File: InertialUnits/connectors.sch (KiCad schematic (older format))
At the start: 2 parts, among them P1 CONN_2, P2 CONN_2

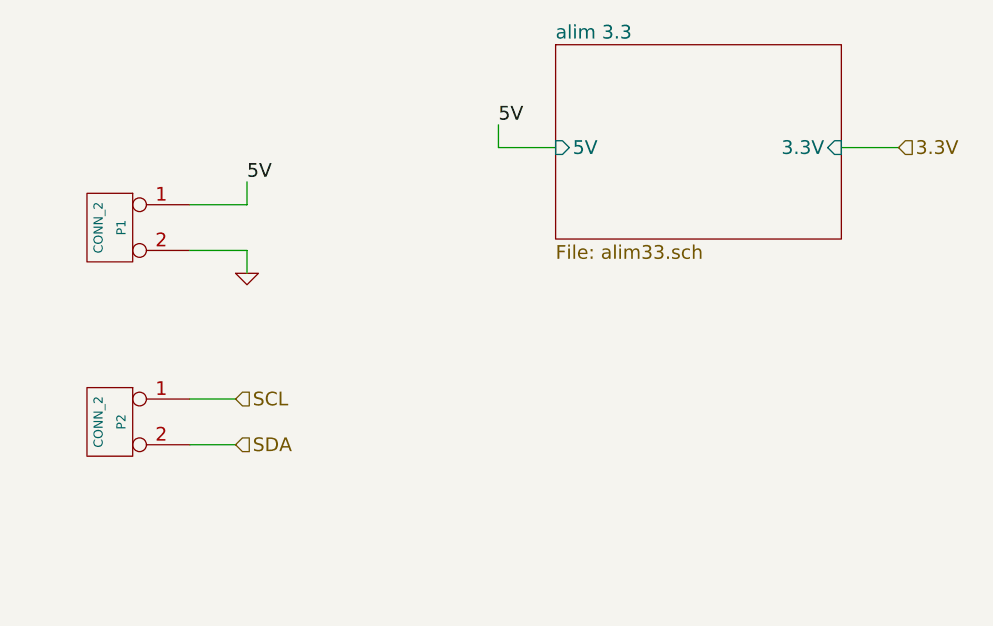
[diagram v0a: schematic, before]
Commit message: Modification axis on Inertial sensors
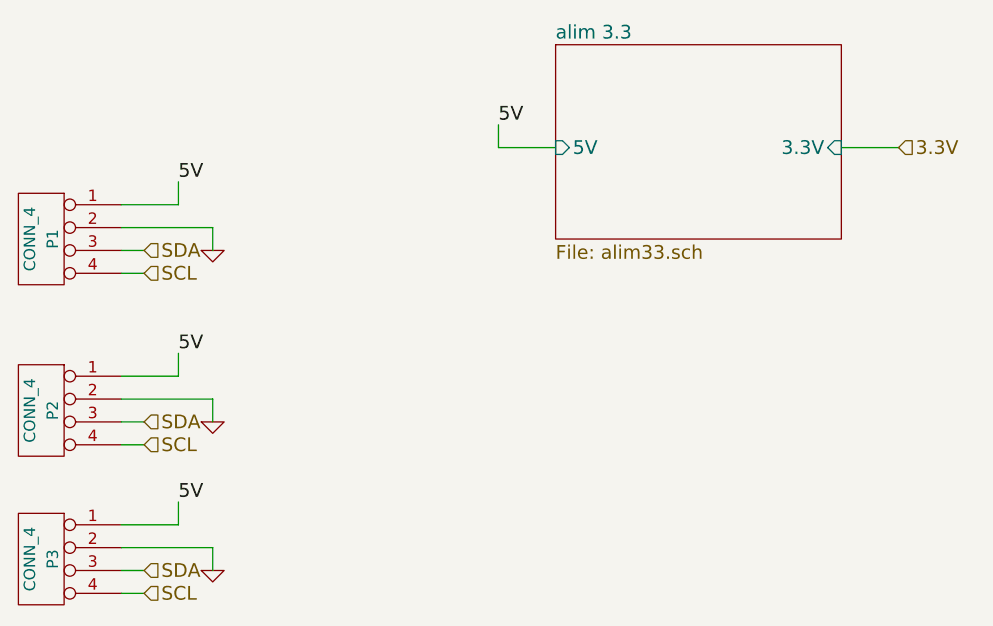
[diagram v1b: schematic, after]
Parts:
- removed P1, P2: CONN_2, symbol CONN_2
- added P1, P2, P3: CONN_4, symbol CONN_4
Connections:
- net 5V: now also P1.1 (P1), P2.1 (P1), P3.1 (P1)
- net GND: now also P1.2 (P2), P2.2 (P2), P3.2 (P2)
- net SCL: now also P1.4 (P4), P2.4 (P4), P3.4 (P4)
- net SDA: now also P1.3 (P3), P2.3 (P3), P3.3 (P3)
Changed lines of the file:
@@
-EESchema Schematic File Version 2  date lun. 31 mars 2014 21:58:22 CEST
+EESchema Schematic File Version 2
 LIBS:power
 LIBS:device
@@
 LIBS:perso
 LIBS:inertialSensors-cache
-EELAYER 25  0
+EELAYER 24 0
 EELAYER END
-$Descr A4 11700 8267
+$Descr A4 11693 8268
 encoding utf-8
 Sheet 2 4
@@
 	4500 2600 4750 2600
 Wire Wire Line
-	1650 3900 1850 3900
+	1350 3150 1450 3150
 Wire Wire Line
-	1900 3150 1900 3050
+	1750 3050 1750 2950
 Wire Wire Line
-	1900 3050 1650 3050
+	1750 2950 1350 2950
 Wire Wire Line
-	1650 2850 1900 2850
+	1350 2850 1600 2850
 Wire Wire Line
-	1900 2850 1900 2750
+	1600 2850 1600 2750
 Wire Wire Line
-	1650 3700 1850 3700
+	1350 3050 1450 3050
 Wire Wire Line
 	3250 2600 3000 2600
@@
 F3 "5V" I L 3250 2600 60
 $EndSheet
-Text Label 1900 2750 0    60   ~ 0
+Text Label 1600 2750 0    60   ~ 0
 5V
-Text HLabel 1850 3900 2    60   Input ~ 0
+Text HLabel 1450 3050 2    60   Input ~ 0
 SDA
-Text HLabel 1850 3700 2    60   Input ~ 0
+Text HLabel 1450 3150 2    60   Input ~ 0
 SCL
 $Comp
 L GND #PWR1
 U 1 1 5339C2C1
-P 1900 3150
-F 0 "#PWR1" H 1900 3150 30  0001 C CNN
-F 1 "GND" H 1900 3080 30  0001 C CNN
-	1    1900 3150
+P 1750 3050
+F 0 "#PWR1" H 1750 3050 30  0001 C CNN
+F 1 "GND" H 1750 2980 30  0001 C CNN
+F 2 "" H 1750 3050 60  0001 C CNN
+F 3 "" H 1750 3050 60  0001 C CNN
+	1    1750 3050
 	1    0    0    -1
 $EndComp
 $Comp
-L CONN_2 P2
-U 1 1 5339C2A9
-P 1300 3800
-F 0 "P2" V 1250 3800 40  0000 C CNN
-F 1 "CONN_2" V 1350 3800 40  0000 C CNN
-	1    1300 3800
+L CONN_4 P1
+U 1 1 534E5AC9
+P 1000 3000
+F 0 "P1" V 950 3000 50  0000 C CNN
+F 1 "CONN_4" V 1050 3000 50  0000 C CNN
+F 2 "" H 1000 3000 60  0000 C CNN
+F 3 "" H 1000 3000 60  0000 C CNN
+	1    1000 3000
 	-1   0    0    -1
 $EndComp
+Wire Wire Line
+	1350 3900 1450 3900
+Wire Wire Line
+	1750 3800 1750 3700
+Wire Wire Line
+	1750 3700 1350 3700
+Wire Wire Line
+	1350 3600 1600 3600
+Wire Wire Line
+	1600 3600 1600 3500
+Wire Wire Line
+	1350 3800 1450 3800
+Text Label 1600 3500 0    60   ~ 0
+5V
+Text HLabel 1450 3800 2    60   Input ~ 0
+SDA
+Text HLabel 1450 3900 2    60   Input ~ 0
+SCL
 $Comp
-L CONN_2 P1
-U 1 1 5339C2A1
-P 1300 2950
-F 0 "P1" V 1250 2950 40  0000 C CNN
-F 1 "CONN_2" V 1350 2950 40  0000 C CNN
-	1    1300 2950
+L GND #PWR2
+U 1 1 534E5B6F
+P 1750 3800
+F 0 "#PWR2" H 1750 3800 30  0001 C CNN
+F 1 "GND" H 1750 3730 30  0001 C CNN
+F 2 "" H 1750 3800 60  0001 C CNN
+F 3 "" H 1750 3800 60  0001 C CNN
+	1    1750 3800
+	1    0    0    -1
+$EndComp
+$Comp
+L CONN_4 P2
+U 1 1 534E5B75
+P 1000 3750
+F 0 "P2" V 950 3750 50  0000 C CNN
+F 1 "CONN_4" V 1050 3750 50  0000 C CNN
+F 2 "" H 1000 3750 60  0000 C CNN
+F 3 "" H 1000 3750 60  0000 C CNN
+	1    1000 3750
 	-1   0    0    -1
 $EndComp
+Wire Wire Line
+	1350 4550 1450 4550
+Wire Wire Line
+	1750 4450 1750 4350
+Wire Wire Line
+	1750 4350 1350 4350
+Wire Wire Line
+	1350 4250 1600 4250
+Wire Wire Line
+	1600 4250 1600 4150
+Wire Wire Line
+	1350 4450 1450 4450
+Text Label 1600 4150 0    60   ~ 0
+5V
+Text HLabel 1450 4450 2    60   Input ~ 0
+SDA
+Text HLabel 1450 4550 2    60   Input ~ 0
+SCL
+$Comp
+L GND #PWR3
+U 1 1 534E5B8A
+P 1750 4450
+F 0 "#PWR3" H 1750 4450 30  0001 C CNN
+F 1 "GND" H 1750 4380 30  0001 C CNN
+F 2 "" H 1750 4450 60  0001 C CNN
+F 3 "" H 1750 4450 60  0001 C CNN
+	1    1750 4450
+	1    0    0    -1
+$EndComp
+$Comp
+L CONN_4 P3
+U 1 1 534E5B90
+P 1000 4400
+F 0 "P3" V 950 4400 50  0000 C CNN
+F 1 "CONN_4" V 1050 4400 50  0000 C CNN
+F 2 "" H 1000 4400 60  0000 C CNN
+F 3 "" H 1000 4400 60  0000 C CNN
+	1    1000 4400
+	-1   0    0    -1
+$EndComp
